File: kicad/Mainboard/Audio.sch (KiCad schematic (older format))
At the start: 61 parts, among them J10 SPK_INT, J11 SPK_EXT, J8 MIC_INT, J9 MIC_EXT, SW1 INT_PTT_SW, U7 OPA340UA, U8 LM386

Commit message: Annotated parts, again.
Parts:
- gave numbers to parts that had none: 16
- renumbered 2k2 to 2k1, C50 to C76, C49 to C78, C46 to C79, C47 to C80, C59 to C81, C58 to C82, C57 to C84, C56 to C85, C53 to C86, C51 to C87, C60 to C88, C55 to C89, C48 to C90, C52 to C91, D2 to D3, D3 to D4, FB3 to FB4, J9 to J10, J10 to J11, J11 to J12, J8 to J9, R16 to R35, R17 to R36, R10 to R37, R14 to R38, R12 to R39, R11 to R40, R24 to R41, R27 to R42, R28 to R43, R18 to R44, R19 to R45, R26 to R46, R13 to R47, R15 to R48, R20 to R49, R21 to R50, U8 to U10, U7 to U9

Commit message: Started assigning footprints
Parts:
- C72, C74: footprint (none) -> Capacitor_SMD:C_0603_1608Metric; symbol Device:C_Small -> Mainboard-rescue:C_Small-Device
- C73, C75, C76, C77, C78, C79, C80, C81, C82, C83, C84, C85, C87, C88, C90, C91: footprint (none) -> Capacitor_SMD:C_0603_1608Metric
- C86, C89: footprint (none) -> Capacitor_Tantalum_SMD:CP_EIA-7343-31_Kemet-D; Partno (none) -> TCJD227M016R0050
- D3, D4: footprint (none) -> Diode_SMD:D_0603_1608Metric
- FB3, FB4: footprint (none) -> Inductor_SMD:L_0603_1608Metric
- R57: renamed from 2k1; value TBD -> 2k1
- RV1: symbol Device:R_POT -> Mainboard-rescue:R_POT-Device
- U8: symbol 4xxx:4066 -> Mainboard-rescue:4066-4xxx
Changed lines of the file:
@@
 F 0 "C78" H 5242 2146 50  0000 L CNN
 F 1 "6n8" H 5242 2055 50  0000 L CNN
-F 2 "" H 5150 2100 50  0001 C CNN
+F 2 "Capacitor_SMD:C_0603_1608Metric" H 5150 2100 50  0001 C CNN
 F 3 "~" H 5150 2100 50  0001 C CNN
 	1    5150 2100
@@
 F 0 "C80" V 5850 1900 50  0000 C CNN
 F 1 "1u" V 5950 1900 50  0000 C CNN
-F 2 "" H 5750 1900 50  0001 C CNN
+F 2 "Capacitor_SMD:C_0603_1608Metric" H 5750 1900 50  0001 C CNN
 F 3 "~" H 5750 1900 50  0001 C CNN
 	1    5750 1900
@@
 F 0 "C79" V 5521 1150 50  0000 C CNN
 F 1 "10u" V 5612 1150 50  0000 C CNN
-F 2 "" H 5750 1150 50  0001 C CNN
+F 2 "Capacitor_SMD:C_0603_1608Metric" H 5750 1150 50  0001 C CNN
 F 3 "~" H 5750 1150 50  0001 C CNN
 	1    5750 1150
@@
 F 0 "C76" H 5042 3446 50  0000 L CNN
 F 1 "22u" H 5042 3355 50  0000 L CNN
-F 2 "" H 4950 3400 50  0001 C CNN
+F 2 "Capacitor_SMD:C_0603_1608Metric" H 4950 3400 50  0001 C CNN
 F 3 "~" H 4950 3400 50  0001 C CNN
 	1    4950 3400
@@
 F 0 "C87" H 8108 3604 50  0000 R CNN
 F 1 "10u" H 8108 3695 50  0000 R CNN
-F 2 "" H 8200 3650 50  0001 C CNN
+F 2 "Capacitor_SMD:C_0603_1608Metric" H 8200 3650 50  0001 C CNN
 F 3 "~" H 8200 3650 50  0001 C CNN
 	1    8200 3650
@@
 F 0 "C90" H 9758 1554 50  0000 R CNN
 F 1 "100n" H 9758 1645 50  0000 R CNN
-F 2 "" H 9850 1600 50  0001 C CNN
+F 2 "Capacitor_SMD:C_0603_1608Metric" H 9850 1600 50  0001 C CNN
 F 3 "~" H 9850 1600 50  0001 C CNN
 	1    9850 1600
@@
 F 0 "FB4" V 6713 3750 50  0000 C CNN
 F 1 "TBD" V 6804 3750 50  0000 C CNN
-F 2 "" V 6880 3750 50  0001 C CNN
+F 2 "Inductor_SMD:L_0603_1608Metric" V 6880 3750 50  0001 C CNN
 F 3 "~" H 6950 3750 50  0001 C CNN
 	1    6950 3750
@@
 F 0 "C82" H 6842 3996 50  0000 L CNN
 F 1 "10n" H 6842 3905 50  0000 L CNN
-F 2 "" H 6750 3950 50  0001 C CNN
+F 2 "Capacitor_SMD:C_0603_1608Metric" H 6750 3950 50  0001 C CNN
 F 3 "~" H 6750 3950 50  0001 C CNN
 	1    6750 3950
@@
 F 0 "C84" H 7242 3996 50  0000 L CNN
 F 1 "1u" H 7242 3905 50  0000 L CNN
-F 2 "" H 7150 3950 50  0001 C CNN
+F 2 "Capacitor_SMD:C_0603_1608Metric" H 7150 3950 50  0001 C CNN
 F 3 "~" H 7150 3950 50  0001 C CNN
 	1    7150 3950
@@
 F 0 "C85" H 7592 3996 50  0000 L CNN
 F 1 "100n" H 7592 3905 50  0000 L CNN
-F 2 "" H 7500 3950 50  0001 C CNN
+F 2 "Capacitor_SMD:C_0603_1608Metric" H 7500 3950 50  0001 C CNN
 F 3 "~" H 7500 3950 50  0001 C CNN
 	1    7500 3950
@@
 F 0 "D3" V 7604 1398 50  0000 L CNN
 F 1 "RED" V 7695 1398 50  0000 L CNN
-F 2 "" V 7650 1300 50  0001 C CNN
+F 2 "Diode_SMD:D_0603_1608Metric" V 7650 1300 50  0001 C CNN
 F 3 "~" V 7650 1300 50  0001 C CNN
 	1    7650 1300
@@
 F 0 "D4" V 8104 1398 50  0000 L CNN
 F 1 "GREEN" V 8195 1398 50  0000 L CNN
-F 2 "" V 8150 1300 50  0001 C CNN
+F 2 "Diode_SMD:D_0603_1608Metric" V 8150 1300 50  0001 C CNN
 F 3 "~" V 8150 1300 50  0001 C CNN
 	1    8150 1300
@@
 F 0 "C91" H 10108 4004 50  0000 R CNN
 F 1 "100n" H 10108 4095 50  0000 R CNN
-F 2 "" H 10200 4050 50  0001 C CNN
+F 2 "Capacitor_SMD:C_0603_1608Metric" H 10200 4050 50  0001 C CNN
 F 3 "~" H 10200 4050 50  0001 C CNN
 	1    10200 4050
@@
 $EndComp
 $Comp
-L Mainboard-rescue:R_Small-device 2k1
+L Mainboard-rescue:R_Small-device R57
 U 1 1 5E095AB1
 P 6350 5200
-F 0 "2k1" H 6409 5246 50  0000 L CNN
-F 1 "TBD" H 6409 5155 50  0000 L CNN
+F 0 "R57" H 6409 5246 50  0000 L CNN
+F 1 "2k1" H 6409 5155 50  0000 L CNN
 F 2 "" H 6350 5200 50  0001 C CNN
 F 3 "~" H 6350 5200 50  0001 C CNN
@@
 F 0 "C81" H 6742 5246 50  0000 L CNN
 F 1 "15n" H 6742 5155 50  0000 L CNN
-F 2 "" H 6650 5200 50  0001 C CNN
+F 2 "Capacitor_SMD:C_0603_1608Metric" H 6650 5200 50  0001 C CNN
 F 3 "~" H 6650 5200 50  0001 C CNN
 	1    6650 5200
@@
 F 0 "C86" V 8125 4250 50  0000 C CNN
 F 1 "220u" V 8034 4250 50  0000 C CNN
-F 2 "" H 7900 4250 50  0001 C CNN
+F 2 "Capacitor_Tantalum_SMD:CP_EIA-7343-31_Kemet-D" H 7900 4250 50  0001 C CNN
 F 3 "~" H 7900 4250 50  0001 C CNN
+F 4 "TCJD227M016R0050" H 7900 4250 50  0001 C CNN "Partno"
 	1    7900 4250
 	0    -1   -1   0
@@
 F 0 "C89" V 8825 5000 50  0000 C CNN
 F 1 "220u" V 8734 5000 50  0000 C CNN
-F 2 "" H 8600 5000 50  0001 C CNN
+F 2 "Capacitor_Tantalum_SMD:CP_EIA-7343-31_Kemet-D" H 8600 5000 50  0001 C CNN
 F 3 "~" H 8600 5000 50  0001 C CNN
+F 4 "TCJD227M016R0050" H 8600 5000 50  0001 C CNN "Partno"
 	1    8600 5000
 	0    -1   -1   0
@@
 F 0 "C88" H 8308 5154 50  0000 R CNN
 F 1 "47n" H 8308 5245 50  0000 R CNN
-F 2 "" H 8400 5200 50  0001 C CNN
+F 2 "Capacitor_SMD:C_0603_1608Metric" H 8400 5200 50  0001 C CNN
 F 3 "~" H 8400 5200 50  0001 C CNN
 	1    8400 5200
@@
 	7400 5100 7400 5700
 $Comp
-L Device:C_Small C74
+L Mainboard-rescue:C_Small-Device C74
 U 1 1 5E069A61
 P 4500 3250
 F 0 "C74" V 4271 3250 50  0000 C CNN
 F 1 "47n" V 4362 3250 50  0000 C CNN
-F 2 "" H 4500 3250 50  0001 C CNN
+F 2 "Capacitor_SMD:C_0603_1608Metric" H 4500 3250 50  0001 C CNN
 F 3 "~" H 4500 3250 50  0001 C CNN
 	1    4500 3250
@@
 ADC1_0
 $Comp
-L Device:R_POT RV1
+L Mainboard-rescue:R_POT-Device RV1
 U 1 1 5E5198E8
 P 7050 4900
@@
 F 0 "C83" H 6942 4746 50  0000 L CNN
 F 1 "220n" H 6942 4655 50  0000 L CNN
-F 2 "" H 6850 4700 50  0001 C CNN
+F 2 "Capacitor_SMD:C_0603_1608Metric" H 6850 4700 50  0001 C CNN
 F 3 "~" H 6850 4700 50  0001 C CNN
 	1    6850 4700
@@
 ADC3_1
 $Comp
-L Device:C_Small C72
+L Mainboard-rescue:C_Small-Device C72
 U 1 1 5E277B6A
 P 1600 6700
 F 0 "C72" V 1371 6700 50  0000 C CNN
 F 1 "100n" V 1462 6700 50  0000 C CNN
-F 2 "" H 1600 6700 50  0001 C CNN
+F 2 "Capacitor_SMD:C_0603_1608Metric" H 1600 6700 50  0001 C CNN
 F 3 "~" H 1600 6700 50  0001 C CNN
 	1    1600 6700
@@
 	700  7400 700  7650
 $Comp
-L 4xxx:4066 U8
+L Mainboard-rescue:4066-4xxx U8
 U 2 1 5E2FADE2
 P 2600 4700
+AR Path="/5E2FADE2" Ref="U8"  Part="2"
+AR Path="/5DFC2ACA/5E2FADE2" Ref="U8"  Part="2"
 F 0 "U8" H 2600 4527 50  0000 C CNN
 F 1 "4066" H 2600 4436 50  0000 C CNN
@@
 $EndComp
 $Comp
-L 4xxx:4066 U8
+L Mainboard-rescue:4066-4xxx U8
 U 5 1 5E2FBECA
 P 5350 6600
+AR Path="/5E2FBECA" Ref="U8"  Part="5"
+AR Path="/5DFC2ACA/5E2FBECA" Ref="U8"  Part="5"
 F 0 "U8" H 5580 6646 50  0000 L CNN
 F 1 "4066" H 5580 6555 50  0000 L CNN
@@
 $EndComp
 $Comp
-L 4xxx:4066 U8
+L Mainboard-rescue:4066-4xxx U8
 U 4 1 5E30A84B
 P 4650 6550
+AR Path="/5E30A84B" Ref="U8"  Part="4"
+AR Path="/5DFC2ACA/5E30A84B" Ref="U8"  Part="4"
 F 0 "U8" H 4650 6285 50  0000 C CNN
 F 1 "4066" H 4650 6376 50  0000 C CNN
@@
 	2150 6700 2050 6700
 $Comp
-L 4xxx:4066 U8
+L Mainboard-rescue:4066-4xxx U8
 U 3 1 5E309A5A
 P 3900 6550
+AR Path="/5E309A5A" Ref="U8"  Part="3"
+AR Path="/5DFC2ACA/5E309A5A" Ref="U8"  Part="3"
 F 0 "U8" H 3900 6285 50  0000 C CNN
 F 1 "4066" H 3900 6376 50  0000 C CNN
@@
 F 0 "FB3" V 4313 5600 50  0000 C CNN
 F 1 "TBD" V 4404 5600 50  0000 C CNN
-F 2 "" V 4480 5600 50  0001 C CNN
+F 2 "Inductor_SMD:L_0603_1608Metric" V 4480 5600 50  0001 C CNN
 F 3 "~" H 4550 5600 50  0001 C CNN
 	1    4550 5600
@@
 F 0 "C73" H 4442 5846 50  0000 L CNN
 F 1 "10n" H 4442 5755 50  0000 L CNN
-F 2 "" H 4350 5800 50  0001 C CNN
+F 2 "Capacitor_SMD:C_0603_1608Metric" H 4350 5800 50  0001 C CNN
 F 3 "~" H 4350 5800 50  0001 C CNN
 	1    4350 5800
@@
 F 0 "C75" H 4842 5846 50  0000 L CNN
 F 1 "1u" H 4842 5755 50  0000 L CNN
-F 2 "" H 4750 5800 50  0001 C CNN
+F 2 "Capacitor_SMD:C_0603_1608Metric" H 4750 5800 50  0001 C CNN
 F 3 "~" H 4750 5800 50  0001 C CNN
 	1    4750 5800
@@
 F 0 "C77" H 5192 5846 50  0000 L CNN
 F 1 "100n" H 5192 5755 50  0000 L CNN
-F 2 "" H 5100 5800 50  0001 C CNN
+F 2 "Capacitor_SMD:C_0603_1608Metric" H 5100 5800 50  0001 C CNN
 F 3 "~" H 5100 5800 50  0001 C CNN
 	1    5100 5800
@@
 SPK_AMP_SEL
 $Comp
-L 4xxx:4066 U8
+L Mainboard-rescue:4066-4xxx U8
 U 1 1 5E2FA047
 P 2200 4300
+AR Path="/5E2FA047" Ref="U8"  Part="1"
+AR Path="/5DFC2ACA/5E2FA047" Ref="U8"  Part="1"
 F 0 "U8" H 2200 4127 50  0000 C CNN
 F 1 "4066" H 2200 4036 50  0000 C CNN

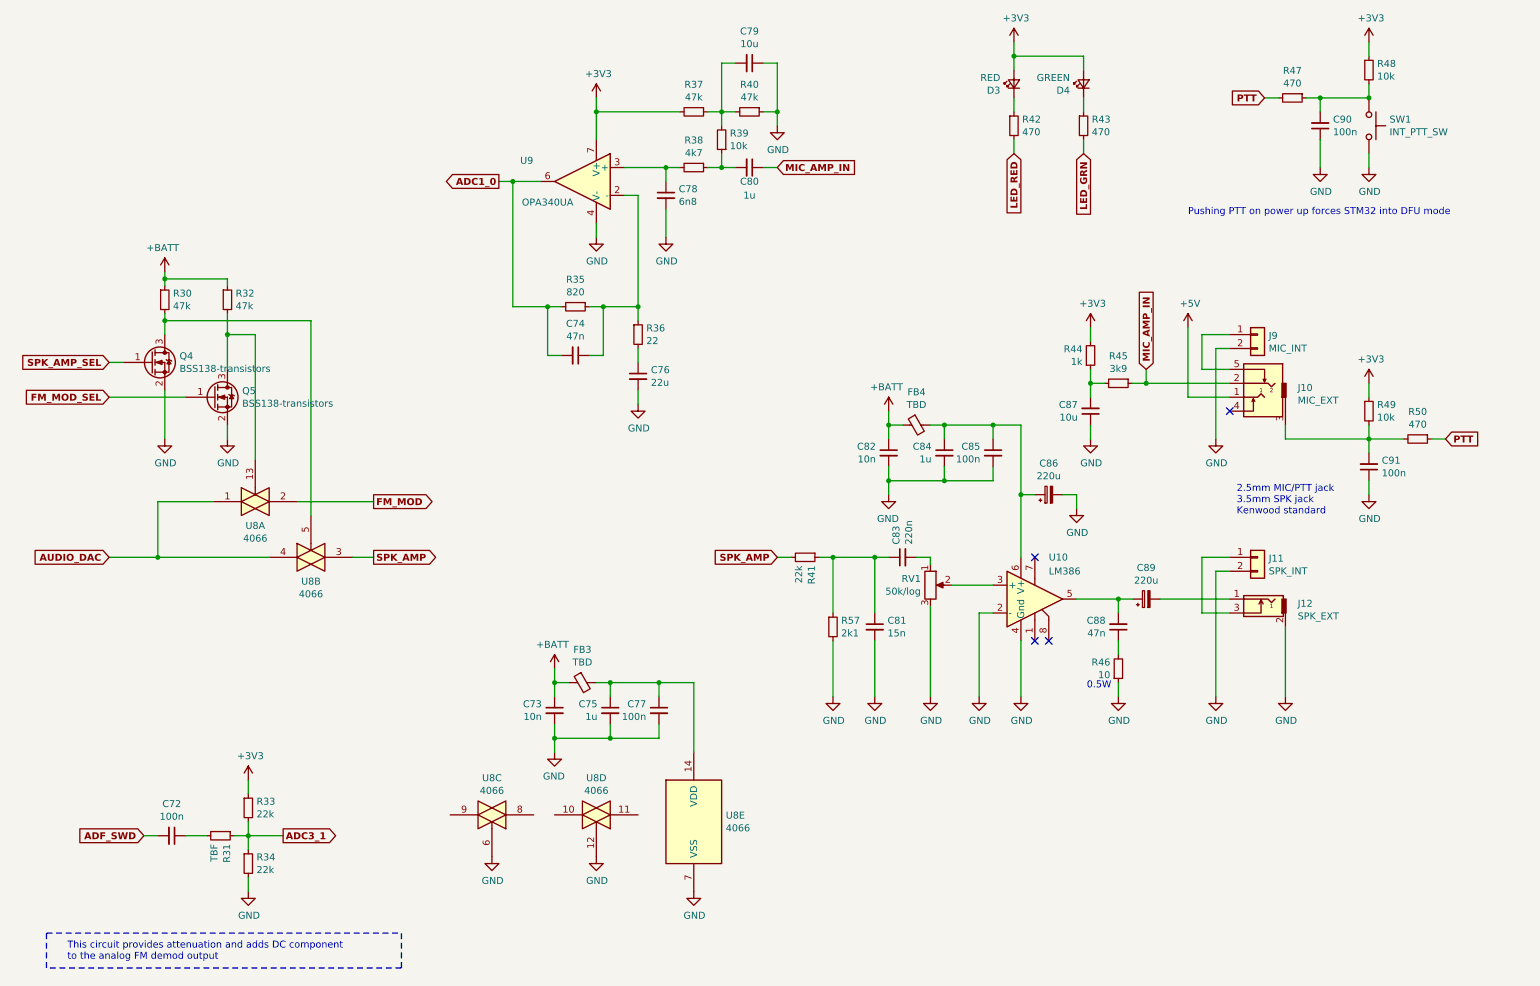
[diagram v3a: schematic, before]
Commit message: Add files via upload
added a Sallen-Key 6kHz anti-aliasing lowpass filter between the ADF (SWD pin) and STM32 (ADC input)
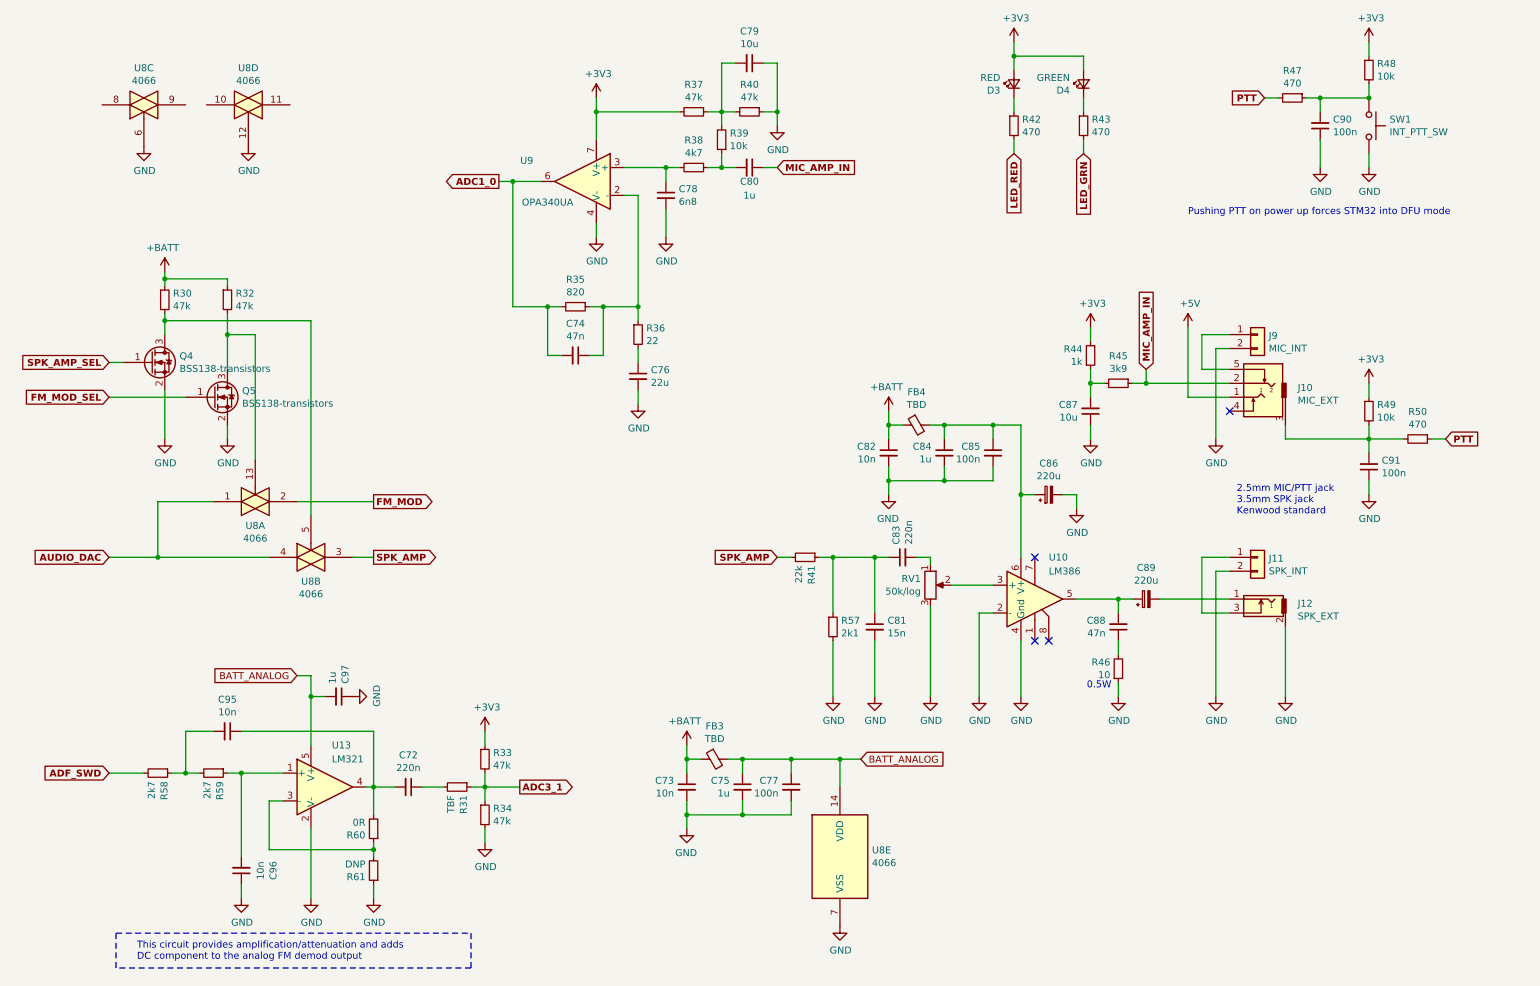
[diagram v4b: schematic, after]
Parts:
- added C95, C96: 10n, Capacitor_SMD:C_0603_1608Metric, symbol Mainboard-rescue:C_Small-Device
- added C97: 1u, Capacitor_SMD:C_0603_1608Metric, symbol Mainboard-rescue:C_Small-device
- added R58, R59: 2k7, symbol Mainboard-rescue:R_Small-device
- added R60: 0R, symbol Mainboard-rescue:R_Small-device
- added R61: DNP, symbol Mainboard-rescue:R_Small-device
- added U13: LM321, Package_TO_SOT_SMD:SOT-23-5, symbol Amplifier_Operational:LM321
- C72: value 100n -> 220n
- R33, R34: value 22k -> 47k
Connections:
- net ADF_SWD: now also R58.2; no longer C72.2
- net GND: now also C96.1, C97.1, R61.1, U13.2 (V-)
- net BATT_ANALOG: now reaches C75.1, C77.1, FB3.2, U8.14 (VDD)
- net BATT_ANALOG: now also C97.2, U13.5 (V+)
- new net: C72.2, C95.1, R60.2, U13.4
- new net: C96.2, R59.1, U13.1 (+)
- new net: R60.1, R61.2, U13.3 (-)
- new net: C95.2, R58.1, R59.2
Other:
- note added: "This circuit provides amplification/attenuation and adds\nDC component to the analog FM demod output"
- note removed: "This circuit provides attenuation and adds DC component\nto the analog FM demod output"
- moved on the sheet: C72, C73, C75, C77, FB3, R31, R33, R34, U8C, U8D, U8E

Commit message: Add files via upload
assigned some more footprints
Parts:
- J11, J9: footprint (none) -> Connector_PinHeader_2.54mm:PinHeader_1x02_P2.54mm_Vertical
- R30, R31, R32, R33, R34, R35, R36, R37, R38, R39, R40, R41, R42, R43, R44, R45, R46, R47, R48, R49, R50, R57, R58, R59, R60, R61: footprint (none) -> Resistor_SMD:R_0603_1608Metric
- RV1: footprint (none) -> Connector_PinHeader_2.54mm:PinHeader_1x03_P2.54mm_Vertical
- U10: footprint (none) -> Package_SO:SOIC-8_3.9x4.9mm_P1.27mm
- U8: value 4066 -> HEF4066B; footprint (none) -> Package_SO:SOIC-14_3.9x8.7mm_P1.27mm
- U9: footprint (none) -> Package_SO:SO-8_3.9x4.9mm_P1.27mm
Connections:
- no-connect marks 4 -> 8
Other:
- moved on the sheet: C73, C75, C77, FB3, U8E

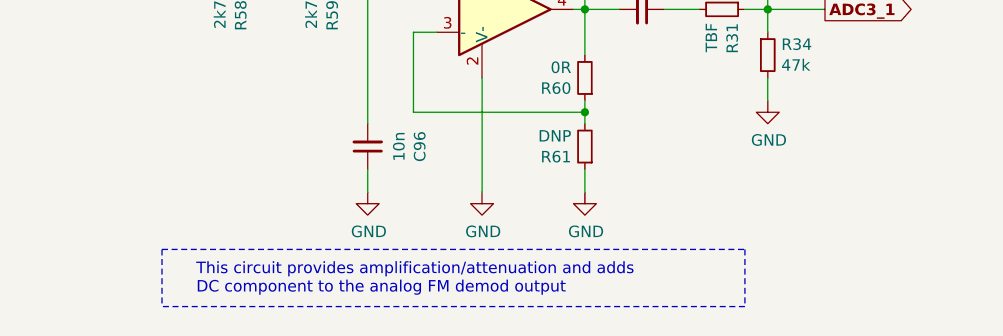
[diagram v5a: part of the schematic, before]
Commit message: Add files via upload
fixed U7 name (LM2904A)
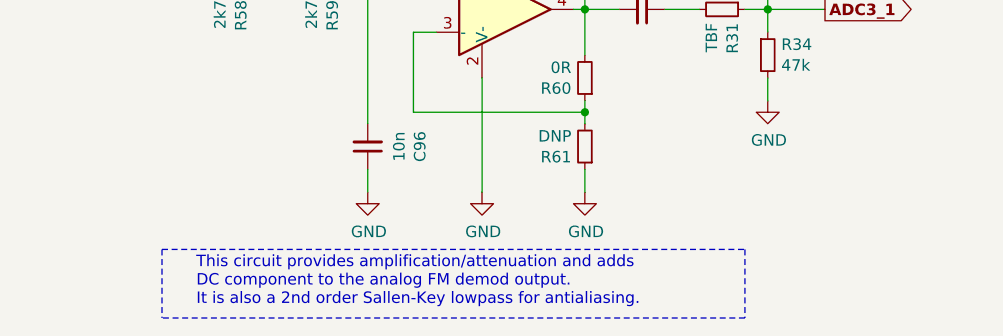
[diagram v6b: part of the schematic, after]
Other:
- note added: "This circuit provides amplification/attenuation and adds\nDC component to the analog FM demod output.\nIt is also a 2nd order Sallen-Key lowpass for antialiasing."
- note removed: "This circuit provides amplification/attenuation and adds\nDC component to the analog FM demod output"
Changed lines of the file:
@@
 	1200 7400 3750 7400
 Wire Notes Line
-	3750 7650 1200 7650
-Wire Notes Line
-	3750 7400 3750 7650
-Wire Notes Line
-	1200 7400 1200 7650
+	3750 7700 1200 7700
 $Comp
 L Mainboard-rescue:4066-4xxx U8
@@
 Wire Wire Line
 	2100 6250 2400 6250
-Text Notes 1350 7600 0    50   ~ 0
-This circuit provides amplification/attenuation and adds\nDC component to the analog FM demod output
+Text Notes 1350 7650 0    50   ~ 0
+This circuit provides amplification/attenuation and adds\nDC component to the analog FM demod output.\nIt is also a 2nd order Sallen-Key lowpass for antialiasing.
 NoConn ~ 1100 1450
 NoConn ~ 1700 1450
 NoConn ~ 1850 1450
 NoConn ~ 2450 1450
+Wire Notes Line
+	1200 7400 1200 7700
+Wire Notes Line
+	3750 7400 3750 7700
 $EndSCHEMATC

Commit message: - Added footprint library - TR-9 - Imported a few footprints - Designed a MicroSD card slot footprint - Assignment footprints to corresponding elements on schematic
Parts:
- J10: footprint (none) -> TR-9:MIC_EXT
- J12: footprint (none) -> TR-9:SPK_EXT
- SW1: footprint (none) -> Button_Switch_THT:SW_Tactile_SKHH_Angled
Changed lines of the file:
@@
 EESchema Schematic File Version 4
-LIBS:Mainboard-cache
 EELAYER 30 0
 EELAYER END
@@
 F 0 "SW1" V 10154 1748 50  0000 L CNN
 F 1 "INT_PTT_SW" V 10245 1748 50  0000 L CNN
-F 2 "" H 10200 1800 50  0001 C CNN
+F 2 "Button_Switch_THT:SW_Tactile_SKHH_Angled" H 10200 1800 50  0001 C CNN
 F 3 "" H 10200 1800 50  0001 C CNN
 	1    10200 1600
@@
 F 0 "J12" H 9112 5168 50  0000 R CNN
 F 1 "SPK_EXT" H 9112 5077 50  0000 R CNN
-F 2 "" H 9650 5200 50  0001 C CNN
+F 2 "TR-9:SPK_EXT" H 9650 5200 50  0001 C CNN
 F 3 "~" H 9650 5200 50  0001 C CNN
 	1    9400 5100
@@
 F 0 "J10" H 9112 3618 50  0000 R CNN
 F 1 "MIC_EXT" H 9112 3527 50  0000 R CNN
-F 2 "" H 9650 3650 50  0001 C CNN
+F 2 "TR-9:MIC_EXT" H 9650 3650 50  0001 C CNN
 F 3 "~" H 9650 3650 50  0001 C CNN
 	1    9400 3550

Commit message: Added HMC RF switch Corrected SOIC footprints assignment
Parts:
- Q4, Q5: footprint TO_SOT_Packages_SMD:SOT-23 -> Package_TO_SOT_SMD:SOT-23
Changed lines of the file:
@@
 F 0 "Q4" H 1656 3346 50  0000 L CNN
 F 1 "BSS138-transistors" H 1656 3255 50  0000 L CNN
-F 2 "TO_SOT_Packages_SMD:SOT-23" H 1650 3225 50  0001 L CIN
+F 2 "Package_TO_SOT_SMD:SOT-23" H 1650 3225 50  0001 L CIN
 F 3 "" H 1450 3300 50  0001 L CNN
 	1    1450 3300
@@
 F 0 "Q5" H 2106 3596 50  0000 L CNN
 F 1 "BSS138-transistors" H 2106 3505 50  0000 L CNN
-F 2 "TO_SOT_Packages_SMD:SOT-23" H 2100 3475 50  0001 L CIN
+F 2 "Package_TO_SOT_SMD:SOT-23" H 2100 3475 50  0001 L CIN
 F 3 "" H 1900 3550 50  0001 L CNN
 	1    1900 3550
